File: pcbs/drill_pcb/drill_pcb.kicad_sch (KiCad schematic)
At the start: 9 parts, among them SW101 RPi reset, U101 PCA9306, U102 Pico

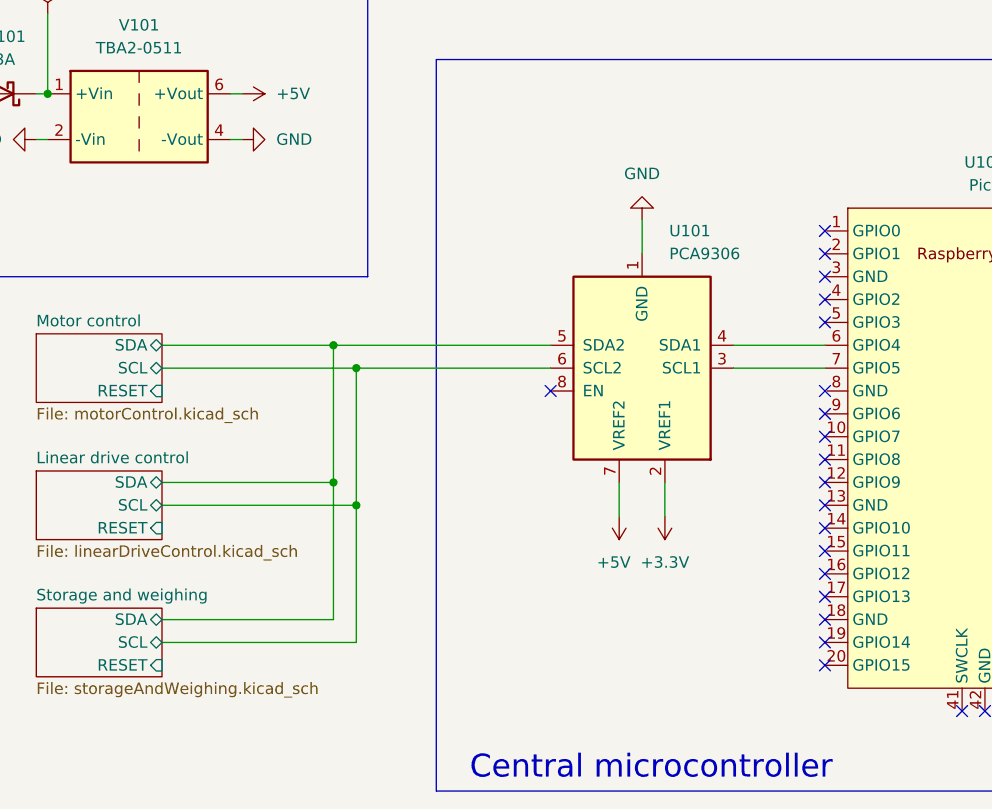
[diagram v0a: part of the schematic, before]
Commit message: add 8ch logic converter
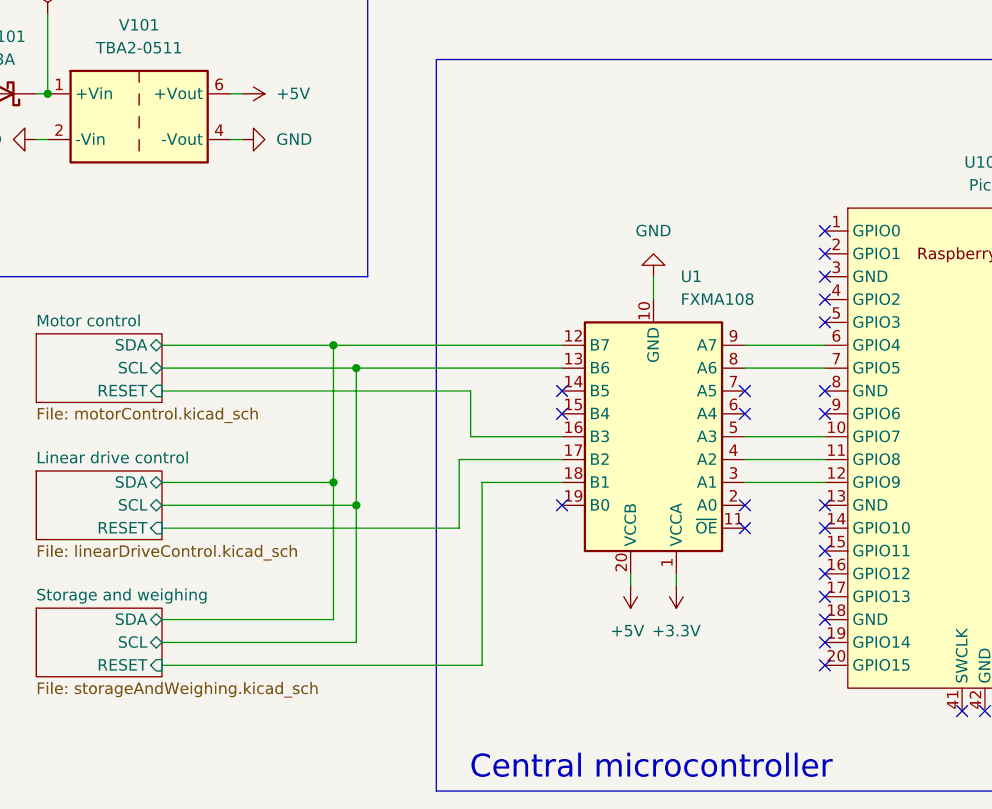
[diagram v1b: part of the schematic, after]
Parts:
- removed U101: PCA9306, drill_i2c_level_shifter:i2c_levl_shifter, symbol Interface:PCA9306
- added U1: FXMA108, drill_i2c_level_shifter:logic_convertor_8ch, symbol Logic_LevelTranslator:FXMA108
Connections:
- net +3.3V: now also U1.1 (VCCA)
- net +5V: now also U1.20 (VCCB)
- net GND: now also U1.10 (GND)
- net Linear drive control/RESET: now also U1.17 (B2)
- net Linear drive control/SCL: now also U1.13 (B6)
- net Linear drive control/SDA: now also U1.12 (B7)
- net Motor control/RESET: now also U1.16 (B3)
- net Storage and weighing/RESET: now also U1.18 (B1)
- net at U102.10 (GPIO7): now also U1.5 (A3)
- net at U102.11 (GPIO8): now also U1.4 (A2)
- net at U102.12 (GPIO9): now also U1.3 (A1)
- net at U102.6 (GPIO4): now also U1.9 (A7)
- net at U102.7 (GPIO5): now also U1.8 (A6)
- no-connect marks 38 -> 41

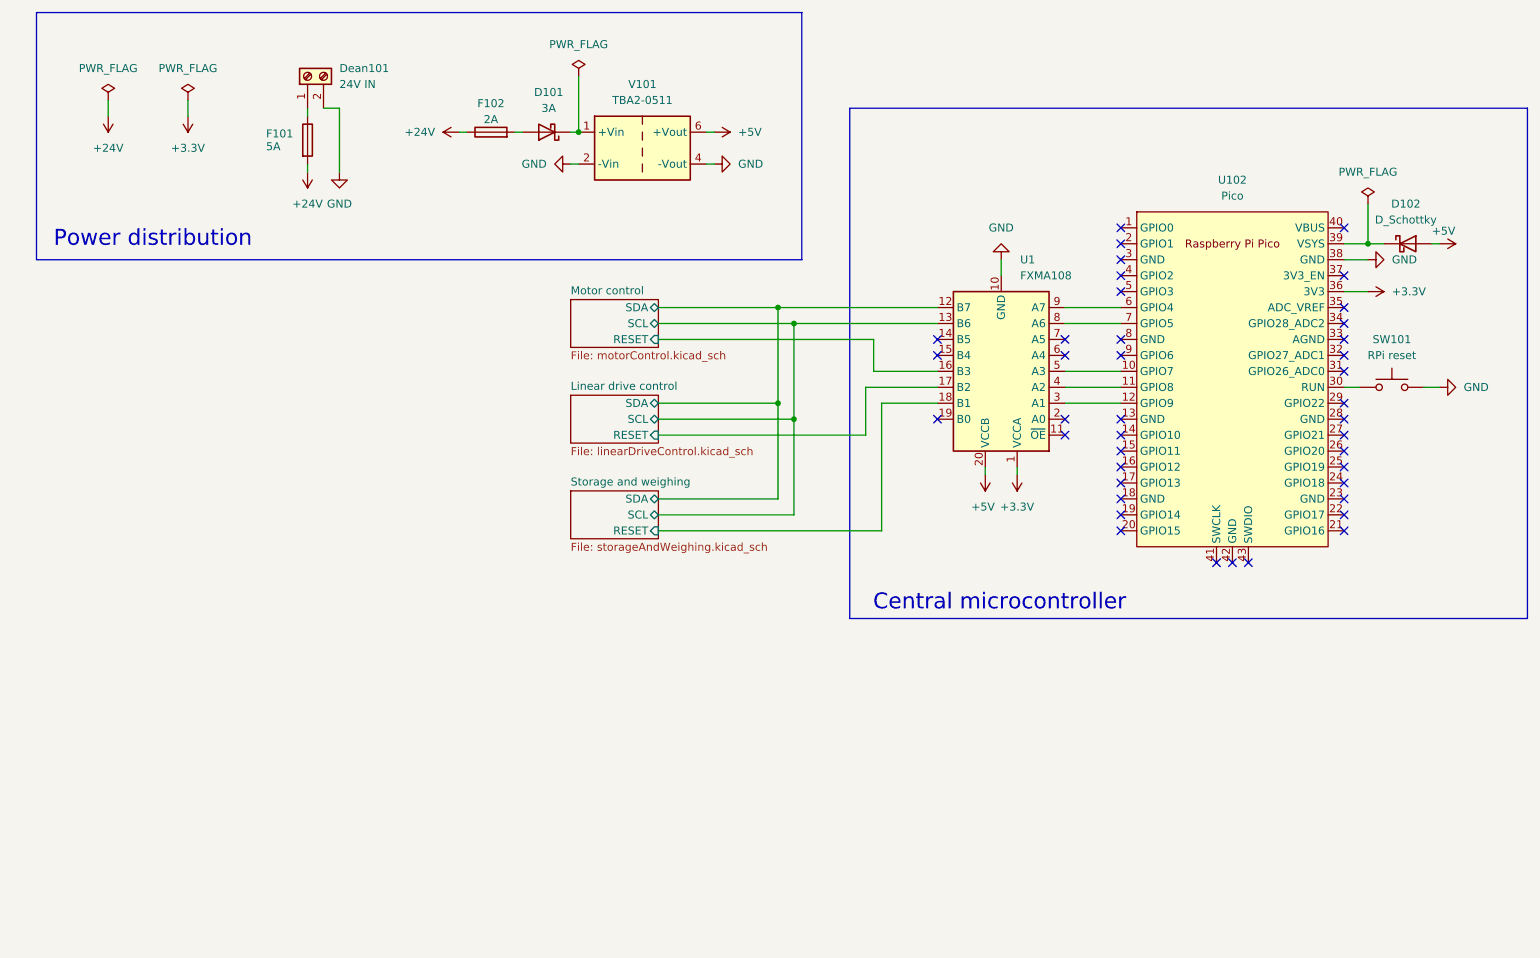
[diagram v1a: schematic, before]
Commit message: Mostly finished PCB v1.0.0 Missing strain gauge control circuit
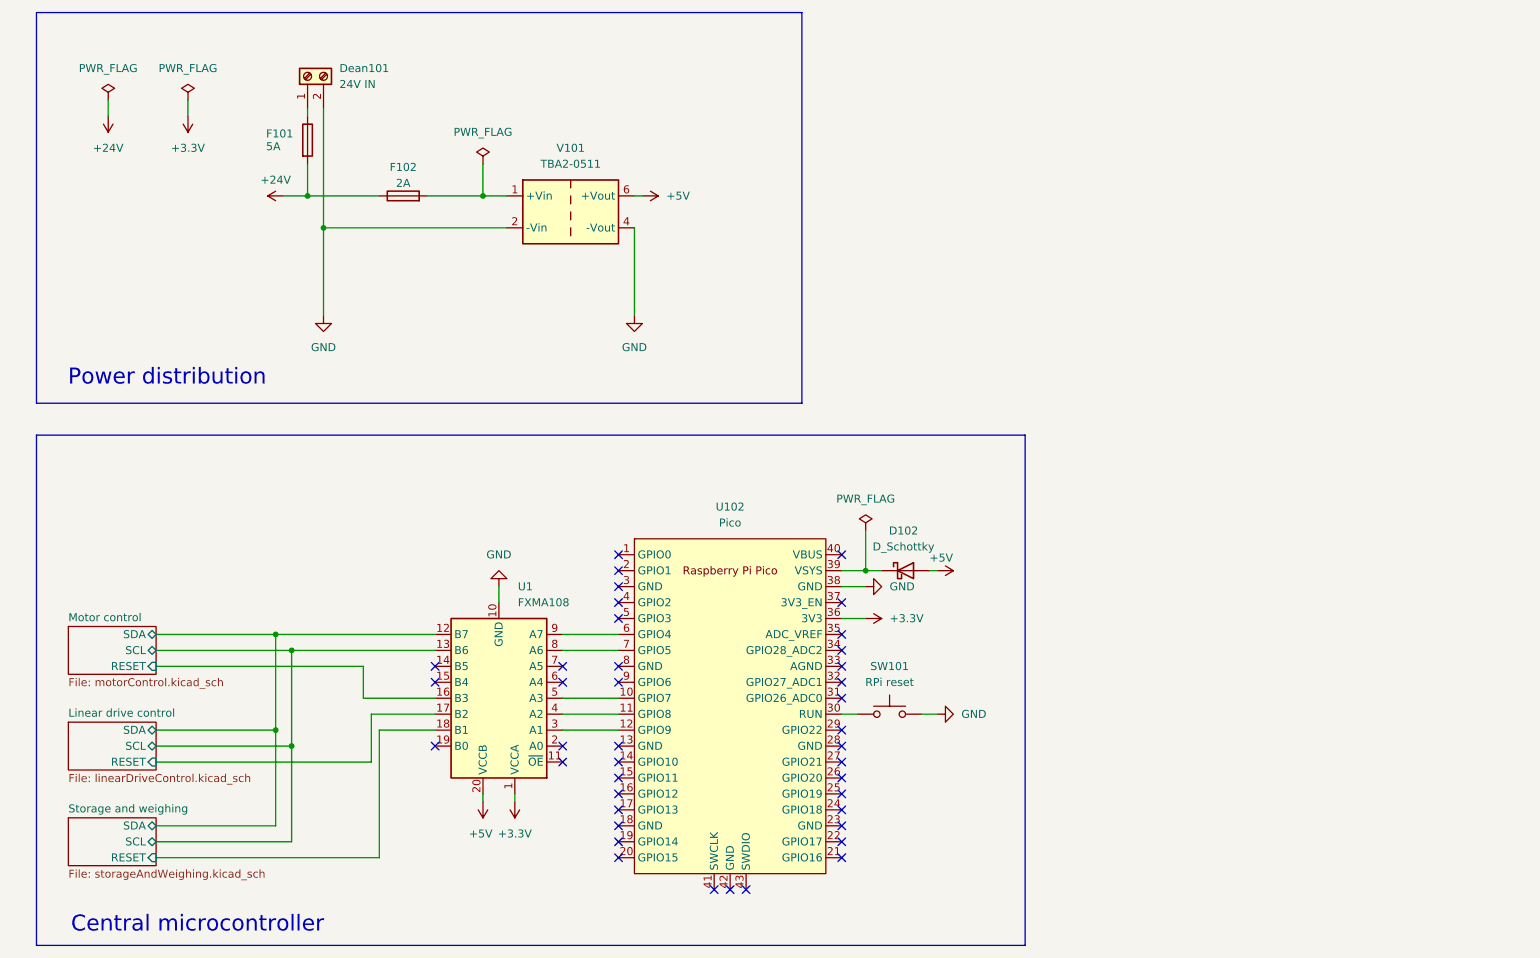
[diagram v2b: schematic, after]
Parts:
- removed D101: 3A, Diode_SMD:D_SMC_Handsoldering, symbol Device:D_Schottky
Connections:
- net at V101.1 (+Vin): now also F102.2
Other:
- moved on the sheet: D102, F102, SW101, U1, U102, V101

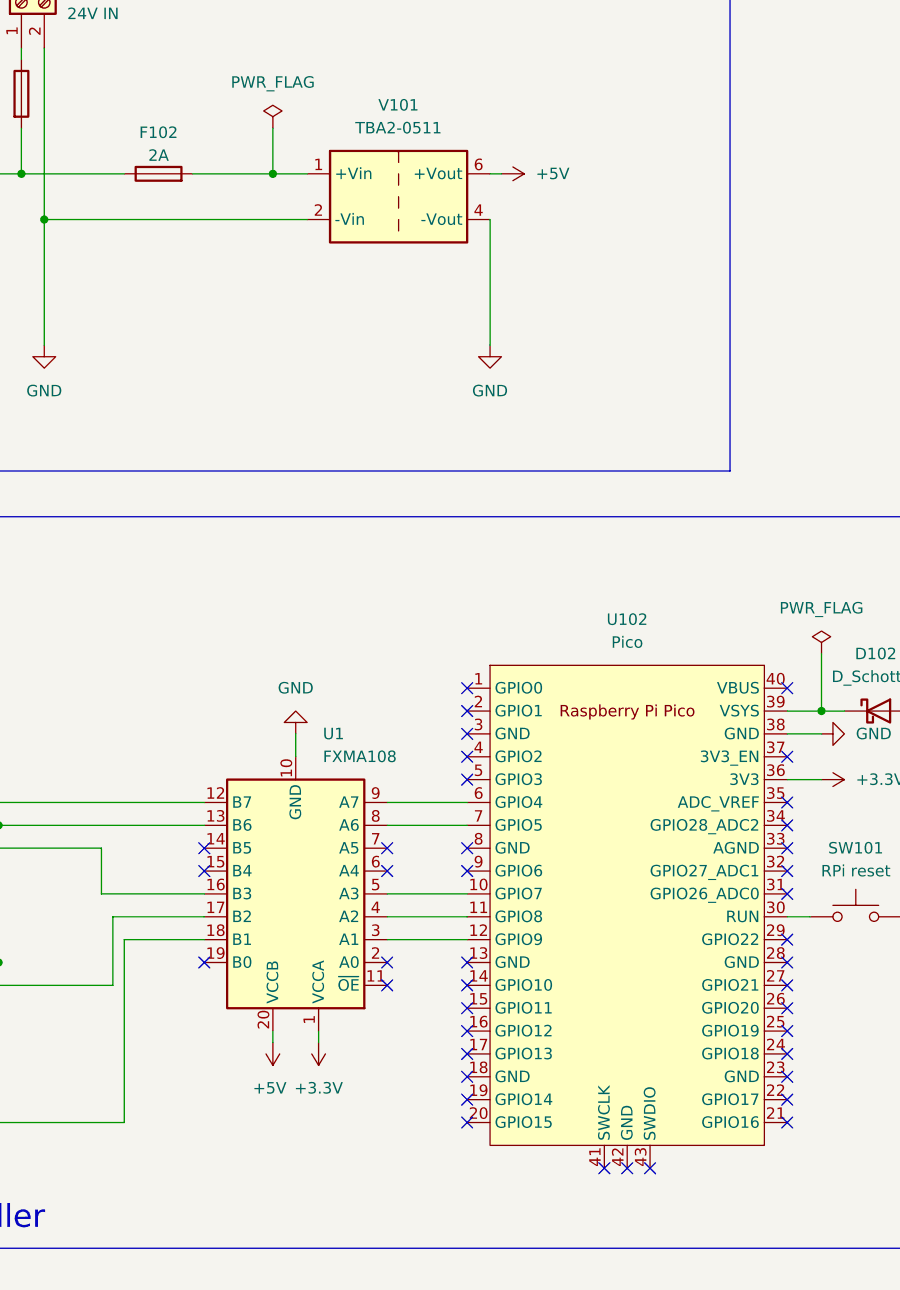
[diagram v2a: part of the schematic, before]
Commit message: PCB update swapped level shifter board for IC
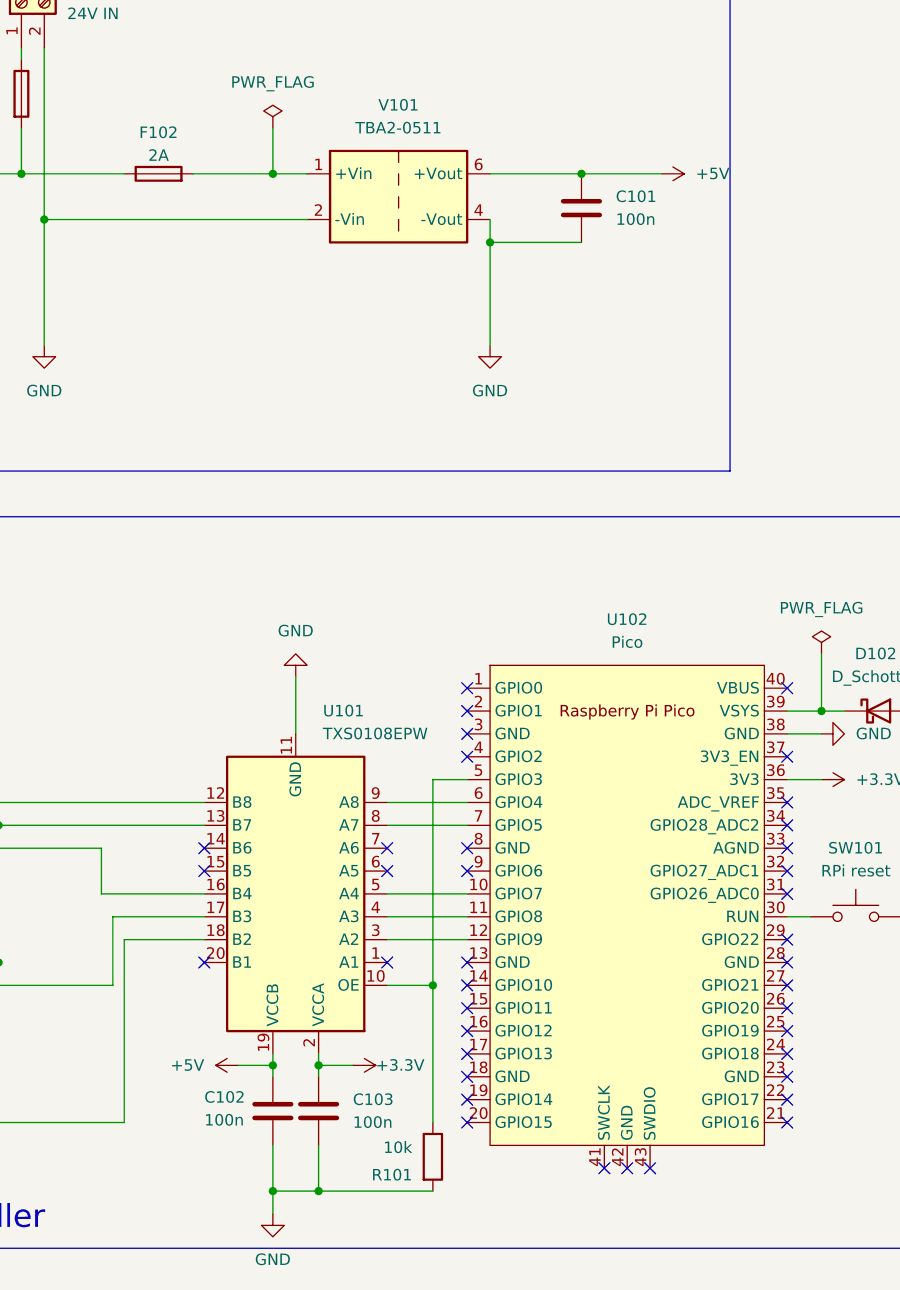
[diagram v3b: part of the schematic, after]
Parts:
- removed U1: FXMA108, drill_i2c_level_shifter:logic_convertor_8ch, symbol Logic_LevelTranslator:FXMA108
- added C101, C102, C103: 100n, Capacitor_SMD:C_1206_3216Metric_Pad1.33x1.80mm_HandSolder, symbol Device:C
- added R101: 10k, Resistor_SMD:R_1206_3216Metric_Pad1.30x1.75mm_HandSolder, symbol Device:R
- added U101: TXS0108EPW, Package_SO:TSSOP-20_4.4x6.5mm_P0.65mm, symbol Logic_LevelTranslator:TXS0108EPW
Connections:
- net +3.3V: now also C103.1, U101.2 (VCCA)
- net +5V: now also C101.1, C102.1, U101.19 (VCCB)
- net GND: now also C101.2, C102.2, C103.2, R101.2, U101.11 (GND)
- net Linear drive control/RESET: now also U101.17 (B3)
- net Linear drive control/SCL: now also U101.13 (B7)
- net Linear drive control/SDA: now also U101.12 (B8)
- net Motor control/RESET: now also U101.16 (B4)
- net Storage and weighing/RESET: now also U101.18 (B2)
- net at U102.10 (GPIO7): now also U101.5 (A4)
- net at U102.11 (GPIO8): now also U101.4 (A3)
- net at U102.12 (GPIO9): now also U101.3 (A2)
- net at U102.5 (GPIO3): now also R101.1, U101.10 (OE)
- net at U102.6 (GPIO4): now also U101.9 (A8)
- net at U102.7 (GPIO5): now also U101.8 (A7)
- no-connect marks 41 -> 39

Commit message: pcb cleanup
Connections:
- net Linear drive control/RESET: no longer names the net of U101.17 (B3)
- net Linear drive control/SCL: no longer names the net of U101.13 (B7)
- net Linear drive control/SDA: no longer names the net of U101.12 (B8)
- net Motor control/RESET: no longer names the net of U101.16 (B4)
- net Storage and weighing/RESET: no longer names the net of U101.18 (B2)
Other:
- removed sheet Linear drive control
- removed sheet Motor control
- removed sheet Storage and weighing
- note removed: "Central microcontroller"
